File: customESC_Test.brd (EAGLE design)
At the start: 160 x 100 mm, 54 parts

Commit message: update
lol
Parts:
- moved MOS6 231.6 mm to (149.9, 25.4), turned to 270 degrees
- moved MOS5 222.9 mm to (149.9, 36.8), turned to 270 degrees
- moved MOS4 213.4 mm to (148.6, 55.9), turned to 270 degrees
- moved DRIV1 213.1 mm to (119.0, 99.1), turned to 270 degrees
- moved R8 209.7 mm to (133.3, 27.9)
- moved H4 209.0 mm to (148.6, 3.81)
- moved MOS3 206.2 mm to (148.6, 67.3), turned to 270 degrees
- moved R7 205.7 mm to (135.0, 39.1)
- moved H3 202.4 mm to (148.6, 123.2)
- moved MOS2 201.5 mm to (148.6, 90.2), turned to 270 degrees
- moved MOS1 196.8 mm to (148.6, 102.9), turned to 270 degrees
- moved R6 195.8 mm to (130.8, 58.4)
- moved R5 195.6 mm to (134.6, 69.8)
- moved D5 191.5 mm to (119.4, 35.6)
- moved R4 188.4 mm to (129.5, 94.0)
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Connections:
- net N$13 renamed VB_3
- net N$3 renamed VB_1
- net N$8 renamed VB_2
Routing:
- net N$14: track 0.00 -> 14.4 mm
- net VCC_2: track 0.00 -> 12.5 mm
- net VB_3: track 0.00 -> 6.88 mm
- net N$16: track 0.00 -> 5.14 mm
- added copper zone on layer 1, net GND
- added copper zone on layer 16, net GND
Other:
- board size 160 x 100 mm -> 152.4 x 127 mm

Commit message: IM DOING WORK AT 4AM
I LOVE ROV!!!!!!!!!!!!!!!!!!!!!!!!!!!!!!!!!!!!!!!!!!!!
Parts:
- moved OUT1 83.4 mm to (138.4, 62.5), turned to 270 degrees
- moved R28 80.1 mm to (48.3, 88.9)
- moved R30 80.1 mm to (40.6, 88.9)
- moved R29 80.1 mm to (43.2, 86.4)
- moved R31 80.1 mm to (62.2, 92.7)
- moved R32 80.1 mm to (58.4, 92.7)
- moved R33 80.1 mm to (54.6, 92.7)
- moved R34 80.1 mm to (50.8, 92.7)
- moved R35 80.1 mm to (47.0, 92.7)
- moved R36 80.1 mm to (43.2, 92.7)
- moved R37 80.1 mm to (39.4, 92.7)
- moved R38 80.1 mm to (35.6, 92.7)
- moved R39 80.1 mm to (31.8, 92.7)
- moved C6 48.7 mm to (97.8, 33.0)
- moved STM1 45.5 mm to (49.5, 58.4)
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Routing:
- net PHASE_C1: track 0.00 -> 108.1 mm, vias 0 -> 2
- net VCC_2: track 12.5 -> 116.8 mm
- net VCC_1: track 0.00 -> 83.4 mm
- net NRST: track 0.00 -> 83.1 mm, vias 0 -> 2
- net PHASE_A1: track 0.00 -> 61.4 mm
- net PHASE_B1: track 0.00 -> 19.2 mm
- net N$7: track 0.00 -> 13.7 mm, vias 0 -> 2
- net N$17: track 0.00 -> 8.17 mm
- net N$15: track 0.00 -> 7.91 mm
- net VB_3: track 6.88 -> 14.5 mm
- net N$2: track 0.00 -> 4.24 mm
- net N$1: track 0.00 -> 3.05 mm
- added copper zone on layer 1, net VCC_1
- added copper zone on layer 1, net VCC_2

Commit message: Catherine Check off
Hello
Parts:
- moved C2 10.2 mm to (101.6, 104.1), turned to 0 degrees
- moved D2 6.35 mm to (57.9, 113.0)
- moved R3 4.02 mm to (105.3, 100.1)
- moved C3 4.02 mm to (83.8, 57.1), turned to 0 degrees
- moved C1 2.84 mm to (83.8, 95.2)
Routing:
- net VCC_2: track 116.8 -> 252.8 mm
- net N$5: track 0.00 -> 6.92 mm
- net N$2: track 4.24 -> 10.6 mm
- net VB_1: track 0.00 -> 5.53 mm

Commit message: Update customESC_Test.brd
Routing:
- net PHASE_C1: track 108.1 -> 111.1 mm
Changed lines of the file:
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@@
 <wire x1="108.585" y1="83.566" x2="109.347" y2="82.804" width="1.016" layer="1"/>
 <wire x1="109.347" y1="82.804" x2="113.0554" y2="82.804" width="1.016" layer="1"/>
-<wire x1="138.43" y1="67.31" x2="138.43" y2="66.675" width="0" layer="19" extent="1-1"/>
-<wire x1="113.919" y1="97.79" x2="119.3165" y2="97.79" width="0" layer="19" extent="1-1"/>
-<wire x1="102.45" y1="104.14" x2="113.919" y2="97.79" width="0" layer="19" extent="1-1"/>
+<wire x1="113.919" y1="97.79" x2="102.45" y2="104.14" width="0" layer="19" extent="1-1"/>
+<wire x1="119.3165" y1="97.79" x2="113.919" y2="97.79" width="0" layer="19" extent="1-1"/>
+<wire x1="138.43" y1="66.675" x2="138.43" y2="67.31" width="0" layer="19" extent="1-1"/>
 <wire x1="94.996" y1="92.71" x2="102.45" y2="104.14" width="0" layer="19" extent="1-1"/>
 <wire x1="63.08" y1="92.71" x2="94.996" y2="92.71" width="0" layer="19" extent="1-1"/>
@@
 <wire x1="104.14" y1="20.32" x2="109.22" y2="20.32" width="1.016" layer="1"/>
 <via x="109.22" y="19.05" extent="1-16" drill="0.35"/>
-<wire x1="119.3165" y1="25.4" x2="138.43" y2="44.5135" width="1.016" layer="1"/>
-<wire x1="138.43" y1="44.5135" x2="138.43" y2="58.293" width="1.016" layer="1"/>
+<wire x1="138.43" y1="39.4335" x2="124.3965" y2="25.4" width="1.016" layer="1"/>
+<wire x1="119.3165" y1="25.4" x2="124.3965" y2="25.4" width="1.016" layer="1"/>
+<wire x1="138.43" y1="39.4335" x2="138.43" y2="58.293" width="1.016" layer="1"/>
 <wire x1="110.236" y1="11.684" x2="109.22" y2="12.7" width="1.016" layer="1"/>
 <via x="109.22" y="12.7" extent="1-16" drill="0.35"/>
@@
 <wire x1="93.915" y1="100.33" x2="94.996" y2="99.249" width="0.762" layer="1"/>
 <wire x1="94.996" y1="99.249" x2="94.996" y2="95.25" width="0.762" layer="1"/>
-<wire x1="94.996" y1="95.25" x2="100.75" y2="104.14" width="0" layer="19" extent="1-1"/>
+<wire x1="93.915" y1="100.33" x2="100.75" y2="104.14" width="0" layer="19" extent="1-1"/>
 </signal>
 <signal name="N$4">
@@
 <wire x1="96.94" y1="33.02" x2="93.98" y2="30.06" width="1.016" layer="1"/>
 <wire x1="93.98" y1="30.06" x2="93.98" y2="24.13" width="1.016" layer="1"/>
-<wire x1="93.915" y1="24.13" x2="95.377" y2="22.668" width="1.016" layer="1"/>
-<wire x1="95.377" y1="22.668" x2="95.377" y2="20.32" width="1.016" layer="1"/>
-<wire x1="93.915" y1="24.13" x2="93.98" y2="24.13" width="0" layer="19" extent="1-1"/>
+<wire x1="93.915" y1="24.13" x2="93.915" y2="22.86" width="1.016" layer="1"/>
+<wire x1="95.377" y1="21.398" x2="93.915" y2="22.86" width="1.016" layer="1"/>
+<wire x1="95.377" y1="21.398" x2="95.377" y2="20.32" width="1.016" layer="1"/>
+<wire x1="95.377" y1="21.398" x2="93.98" y2="24.13" width="0" layer="19" extent="1-1"/>
 </signal>
 </signals>

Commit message: changes
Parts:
- moved D1 2.54 mm to (36.8, 115.6)
- moved D2 2.54 mm to (57.9, 115.6)
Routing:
- net VCC_2: track 252.8 -> 342.1 mm, vias 0 -> 1
- net VCC_1: track 83.4 -> 142.5 mm
- net NRST: track 83.1 -> 94.7 mm
- net PHASE_A1: track 61.4 -> 64.4 mm
- net N$2: track 10.6 -> 8.05 mm
- net N$1: track 3.05 -> 5.59 mm

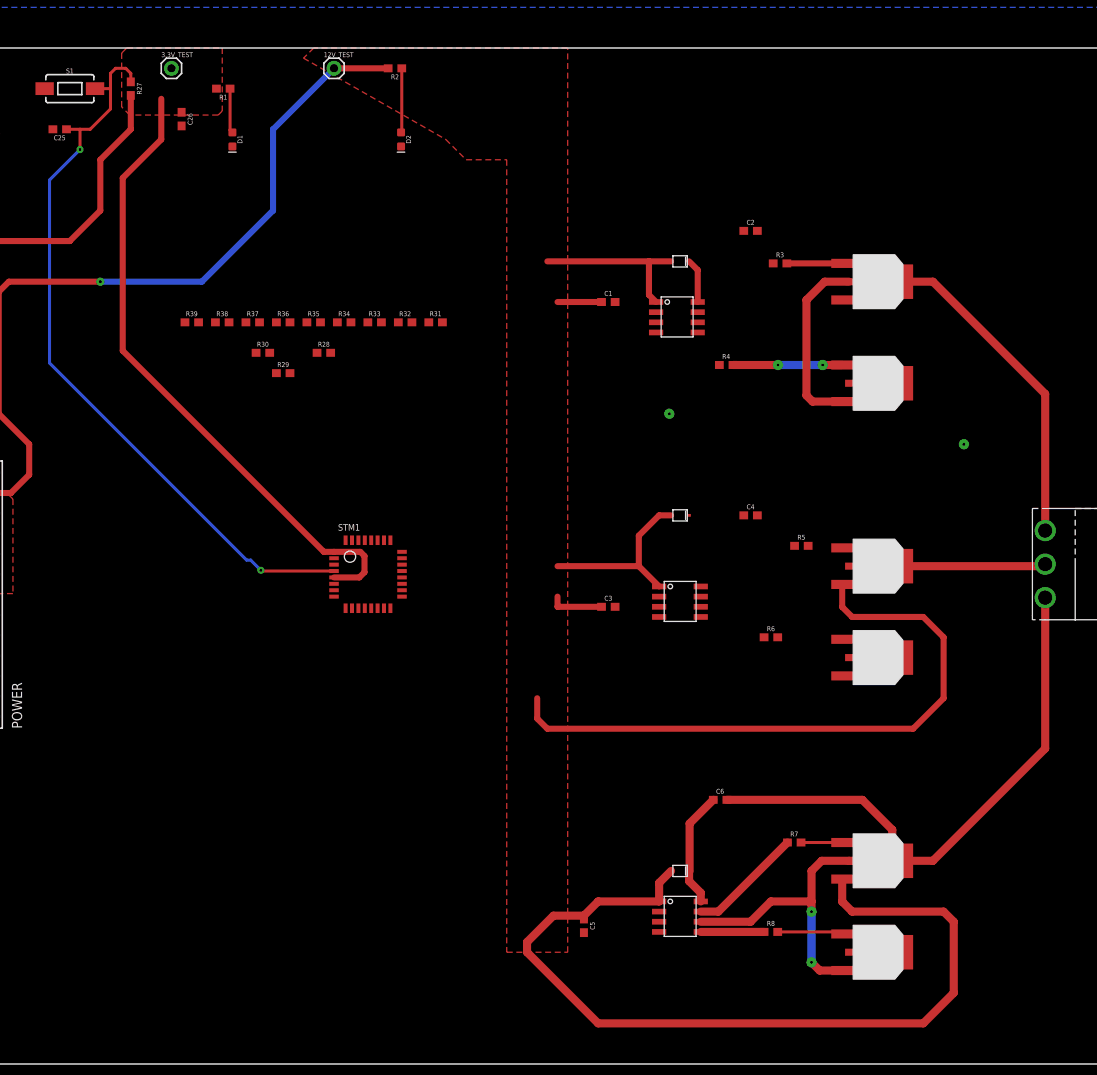
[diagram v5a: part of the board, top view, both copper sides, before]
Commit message: Finished first draft
Need a design review before ordering
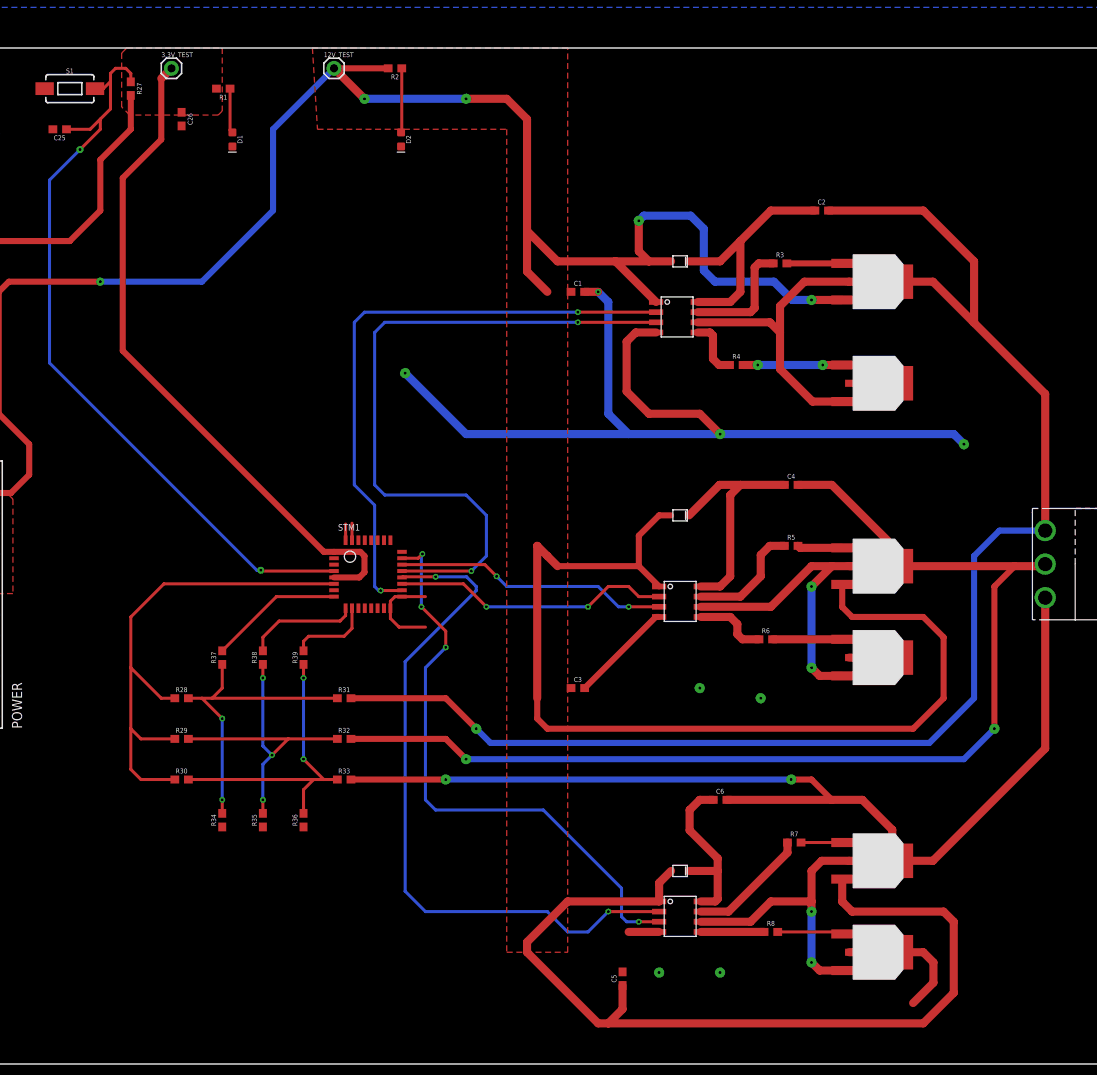
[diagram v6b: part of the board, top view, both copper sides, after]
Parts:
- moved R34 64.1 mm to (35.6, 30.5), turned to 90 degrees
- moved R35 62.6 mm to (40.6, 30.5), turned to 90 degrees
- moved R36 62.3 mm to (45.7, 30.5), turned to 90 degrees
- moved R33 57.3 mm to (50.8, 35.6)
- moved R30 54.3 mm to (30.5, 35.6)
- moved R32 52.6 mm to (50.8, 40.6)
- moved R31 48.4 mm to (50.8, 45.7)
- moved R29 47.5 mm to (30.5, 40.6)
- moved R28 46.7 mm to (30.5, 45.7)
- moved R39 44.2 mm to (45.7, 50.8), turned to 90 degrees
- moved R38 42.2 mm to (40.6, 50.8), turned to 90 degrees
- moved R37 42.1 mm to (35.6, 50.8), turned to 90 degrees
- moved C3 10.9 mm to (80.0, 47.0)
- moved C2 9.25 mm to (110.5, 106.7)
- moved C5 8.18 mm to (85.6, 10.7), turned to 90 degrees
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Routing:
- net GND: track 0.00 -> 175.3 mm, vias 2 -> 8
- net PHASE_B1: track 19.2 -> 190.6 mm, vias 0 -> 4
- net PHASE_A1: track 64.4 -> 224.4 mm, vias 0 -> 1
- net VCC_2: track 342.1 -> 451.5 mm, vias 1 -> 5
- net AL1: track 0.00 -> 86.7 mm, vias 0 -> 2
- net CH1: track 0.00 -> 86.5 mm, vias 0 -> 2
- net AH1: track 0.00 -> 76.0 mm, vias 0 -> 2
- net CL1: track 0.00 -> 73.5 mm, vias 0 -> 4
- net COM1: track 0.00 -> 65.3 mm
- net PHASE_C1: track 111.1 -> 172.3 mm, vias 2 -> 4
- net N$65: track 0.00 -> 41.1 mm, vias 0 -> 3
- net N$66: track 0.00 -> 38.8 mm, vias 0 -> 2
- net N$64: track 0.00 -> 38.8 mm, vias 0 -> 2
- net BH1: track 0.00 -> 34.9 mm, vias 0 -> 2
- net BL1: track 0.00 -> 34.3 mm, vias 0 -> 2
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
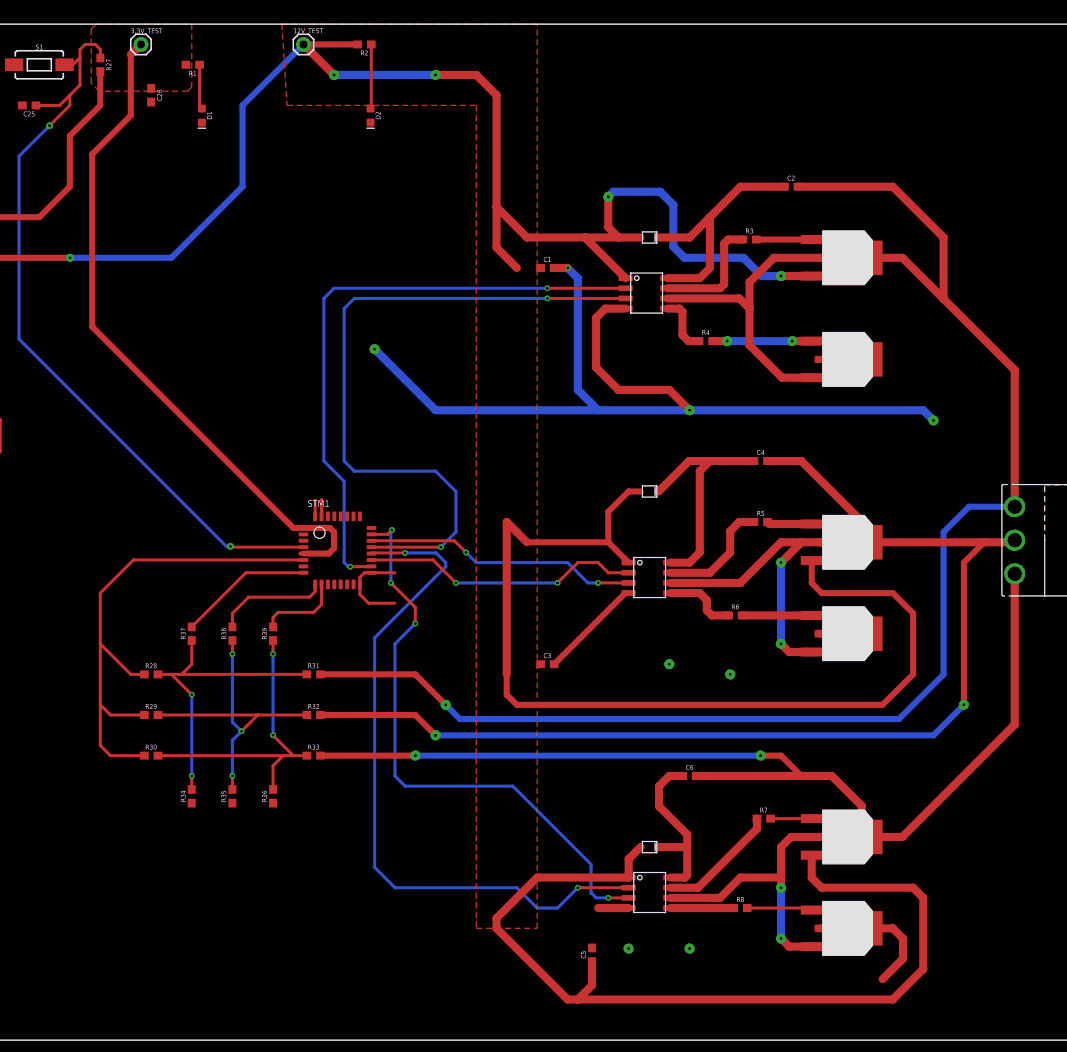
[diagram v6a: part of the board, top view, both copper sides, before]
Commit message: Fixed issues from design review
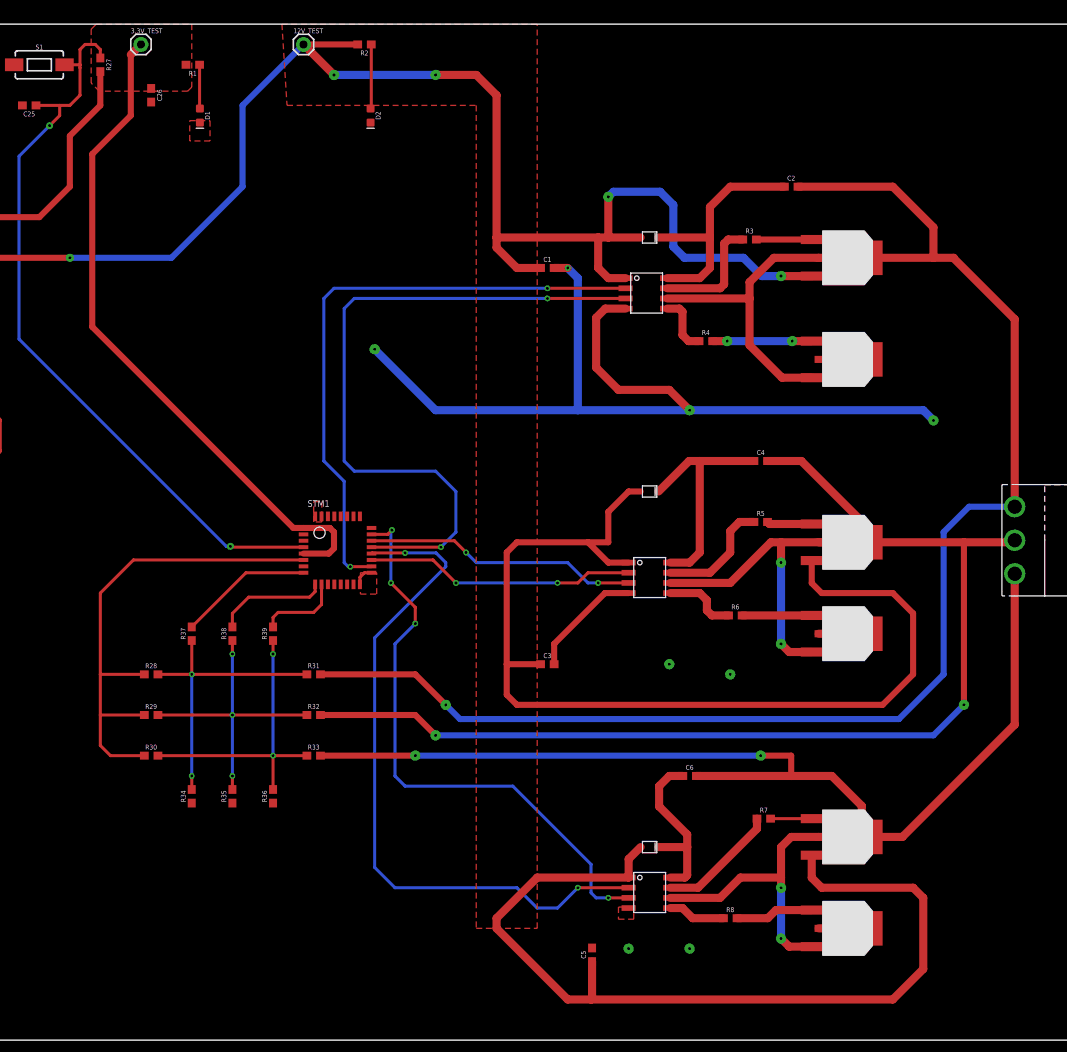
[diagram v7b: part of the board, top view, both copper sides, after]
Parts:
- moved R8 1.80 mm to (102.9, 15.2)
- moved D1 0.25 mm to (36.6, 115.6)
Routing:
- net GND: track 175.3 -> 145.6 mm
- net N$65: track 41.1 -> 37.2 mm
- net VCC_2: track 451.5 -> 454.7 mm
- net PHASE_A1: track 224.4 -> 222.1 mm
- net PHASE_B1: track 190.6 -> 188.5 mm
- net COM1: track 65.3 -> 63.2 mm
- net N$17: track 8.17 -> 9.76 mm
- net N$66: track 38.8 -> 37.2 mm
- net N$64: track 38.8 -> 37.2 mm
- net NRST: track 96.9 -> 95.5 mm
- net BH1: track 34.9 -> 33.9 mm
- net N$15: track 7.91 -> 7.17 mm
- net VB_2: track 29.7 -> 29.1 mm

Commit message: yo
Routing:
- net CL1: track 73.5 -> 72.8 mm
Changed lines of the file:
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@@
 <via x="63.5" y="52.07" extent="1-16" drill="0.35"/>
 <via x="60.452" y="57.15" extent="1-16" drill="0.35"/>
-<wire x1="60.452" y1="57.15" x2="60.452" y2="63.627" width="0.381" layer="16"/>
-<wire x1="60.452" y1="63.627" x2="60.579" y2="63.754" width="0.381" layer="16"/>
-<via x="60.579" y="63.754" extent="1-16" drill="0.35"/>
-<wire x1="60.579" y1="63.754" x2="60.045" y2="63.22" width="0.381" layer="1"/>
-<wire x1="60.045" y1="63.22" x2="58.03" y2="63.22" width="0.381" layer="1"/>
+<wire x1="60.579" y1="63.246" x2="60.579" y2="57.277" width="0.381" layer="16"/>
+<wire x1="60.452" y1="57.15" x2="60.579" y2="57.277" width="0.381" layer="16"/>
+<via x="60.579" y="63.246" extent="1-16" drill="0.35"/>
+<wire x1="60.579" y1="63.246" x2="60.553" y2="63.22" width="0.381" layer="1"/>
+<wire x1="60.553" y1="63.22" x2="58.03" y2="63.22" width="0.381" layer="1"/>
 <wire x1="63.5" y1="52.07" x2="63.5" y2="54.102" width="0.381" layer="1"/>
 <wire x1="63.5" y1="54.102" x2="60.452" y2="57.15" width="0.381" layer="1"/>
